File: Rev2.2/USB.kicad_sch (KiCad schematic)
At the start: 3 parts, among them J8 USB_OTG, U6 STMPS2151STR(Current protecti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, U7 USBLC6-2P6(ESD protection)

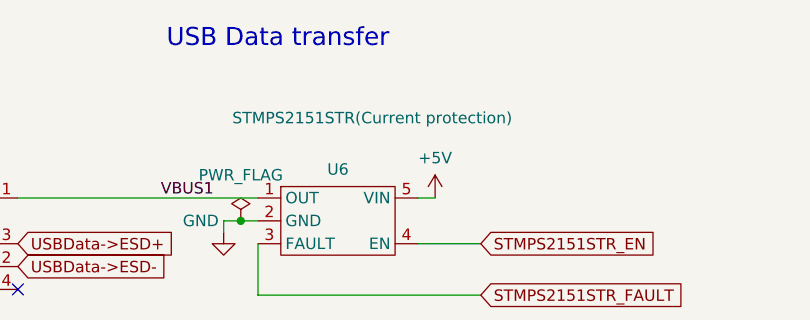
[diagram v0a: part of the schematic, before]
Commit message: changed layer stack up to sig,gnd,gnd, sig/power and routing according to the new stackup
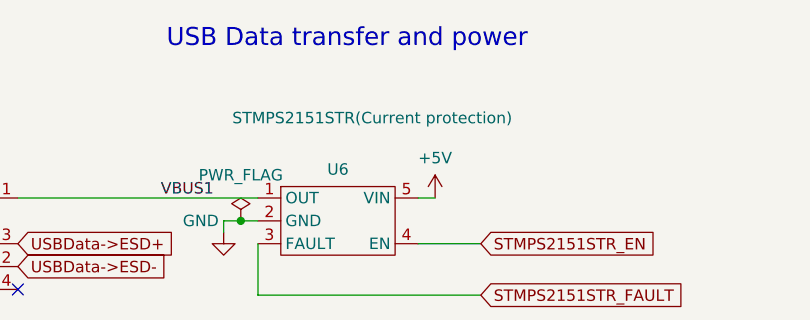
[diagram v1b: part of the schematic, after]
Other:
- note added: "USB Data transfer and power"
- note removed: "USB Data transfer"
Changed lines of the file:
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@@
     )
   )
-  (text "USB Data transfer\n" (at 46.355 19.05 0)
+  (text "USB Data transfer and power\n" (at 46.355 19.05 0)
     (effects (font (size 2 2)) (justify left bottom))
   )

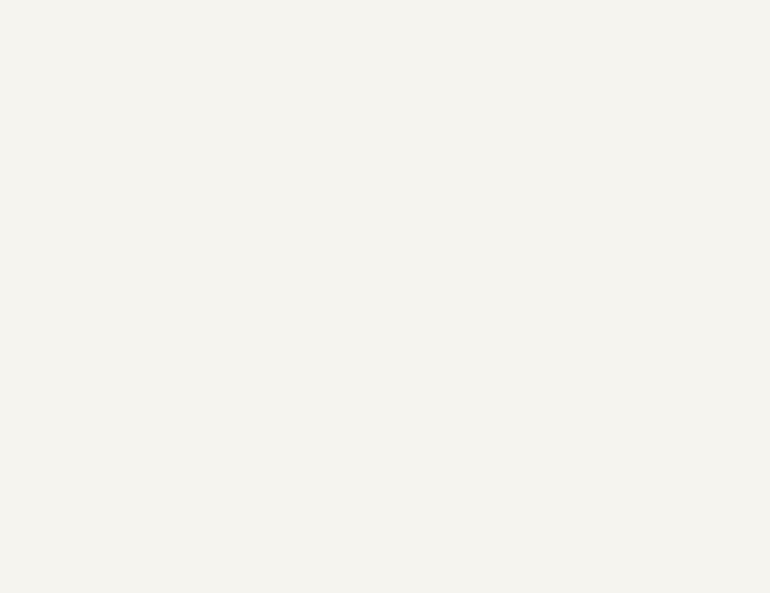
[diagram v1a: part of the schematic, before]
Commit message: added a usb C for power delivery and moved voltage regulator and readjusted the partial power plane to fit the USB C
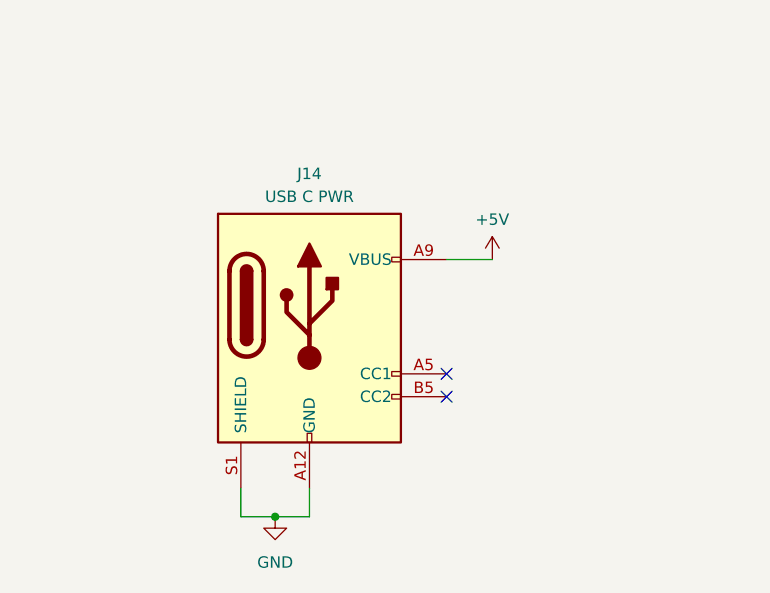
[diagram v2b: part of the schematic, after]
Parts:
- added J14: USB C PWR, Connector_USB:USB_C_Receptacle_GCT_USB4135-GF-A_6P_TopMnt_Horizontal, symbol Connector:USB_C_Receptacle_PowerOnly_6P
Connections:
- net +5V: now also J14.A9 (VBUS), J14.B9 (VBUS)
- net GND: now also J14.A12 (GND), J14.B12 (GND), J14.S1 (SHIELD)
- no-connect marks 1 -> 3
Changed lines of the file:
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@@
   (junction (at 54.61 38.1) (diameter 0) (color 0 0 0 0)
   )
+  (junction (at 40.64 163.83) (diameter 0) (color 0 0 0 0)
+  )
   (junction (at 22.225 53.975) (diameter 0) (color 0 0 0 0)
   )
+  (no_connect (at 59.69 150.495))
+  (no_connect (at 59.69 147.955))
   (no_connect (at 29.845 45.72))
   (wire (pts (xy 52.705 39.37) (xy 52.705 38.1))
     (stroke (width 0) (type default))
   )
+  (wire (pts (xy 40.64 163.83) (xy 44.45 163.83))
+    (stroke (width 0) (type default))
+  )
   (wire (pts (xy 22.225 55.245) (xy 22.225 53.975))
     (stroke (width 0) (type default))
   )
+  (wire (pts (xy 44.45 160.655) (xy 44.45 163.83))
+    (stroke (width 0) (type default))
+  )
   (polyline (pts (xy 12.065 89.535) (xy 285.115 89.535))
     (stroke (width 0) (type default))
@@
     (stroke (width 0) (type default))
   )
+  (wire (pts (xy 36.83 163.83) (xy 40.64 163.83))
+    (stroke (width 0) (type default))
+  )
   (wire (pts (xy 180.34 50.165) (xy 180.34 48.895))
     (stroke (width 0) (type default))
@@
     (stroke (width 0) (type default))
   )
+  (wire (pts (xy 64.77 135.255) (xy 59.69 135.255))
+    (stroke (width 0) (type default))
+  )
   (wire (pts (xy 163.83 38.735) (xy 167.64 38.735))
     (stroke (width 0) (type default))
@@
     (stroke (width 0) (type default))
   )
+  (wire (pts (xy 36.83 160.655) (xy 36.83 163.83))
+    (stroke (width 0) (type default))
+  )
   (wire (pts (xy 52.705 38.1) (xy 54.61 38.1))
     (stroke (width 0) (type default))
@@
     )
   )
+  (symbol (lib_id "Connector:USB_C_Receptacle_PowerOnly_6P") (at 44.45 142.875 0) (unit 1)
+    (in_bom yes) (on_board yes) (dnp no) (fields_autoplaced)
+    (property "Reference" "J14" (at 44.45 125.73 0)
+      (effects (font (size 1.27 1.27)))
+    )
+    (property "Value" "USB C PWR" (at 44.45 128.27 0)
+      (effects (font (size 1.27 1.27)))
+    )
+    (property "Footprint" "Connector_USB:USB_C_Receptacle_GCT_USB4135-GF-A_6P_TopMnt_Horizontal" (at 48.26 140.335 0)
+      (effects (font (size 1.27 1.27)) hide)
+    )
+    (property "Datasheet" "https://www.usb.org/sites/default/files/documents/usb_type-c.zip" (at 44.45 142.875 0)
+      (effects (font (size 1.27 1.27)) hide)
+    )
+    (pin "A12")
+    (pin "A5")
+    (pin "A9")
+    (pin "B12")
+    (pin "B5")
+    (pin "B9")
+    (pin "S1")
+    (instances
+      (project "Rev2.2"
+        (path "/e13dd0ba-f8fd-4ca9-a3d0-94442596488c/4fad712d-8773-4615-bfba-e4cd5d9a6bf4"
+          (reference "J14") (unit 1)
+        )
+      )
+    )
+  )
   (symbol (lib_id "power:GND") (at 22.225 55.245 0) (unit 1)
     (in_bom yes) (on_board yes) (dnp no) (fields_autoplaced)
@@
         )
       )
+    )
+  )
+  (symbol (lib_id "power:+5V") (at 64.77 135.255 0) (unit 1)
+    (in_bom yes) (on_board yes) (dnp no) (fields_autoplaced)
+    (property "Reference" "#PWR059" (at 64.77 139.065 0)
+      (effects (font (size 1.27 1.27)) hide)
+    )
+    (property "Value" "+5V" (at 64.77 130.81 0)
+      (effects (font (size 1.27 1.27)))
+    )
+    (property "Footprint" "" (at 64.77 135.255 0)
+      (effects (font (size 1.27 1.27)) hide)
+    )
+    (property "Datasheet" "" (at 64.77 135.255 0)
+      (effects (font (size 1.27 1.27)) hide)
+    )
+    (pin "1")
+    (instances
+      (project "Rev2.2"
+        (path "/e13dd0ba-f8fd-4ca9-a3d0-94442596488c/4fad712d-8773-4615-bfba-e4cd5d9a6bf4"
+          (reference "#PWR059") (unit 1)
+        )
+      )
+    )
+  )
+  (symbol (lib_id "power:GND") (at 40.64 163.83 0) (unit 1)
+    (in_bom yes) (on_board yes) (dnp no) (fields_autoplaced)
+    (property "Reference" "#PWR060" (at 40.64 170.18 0)
+      (effects (font (size 1.27 1.27)) hide)
+    )
+    (property "Value" "GND" (at 40.64 168.91 0)
+      (effects (font (size 1.27 1.27)))
+    )
+    (property "Footprint" "" (at 40.64 163.83 0)
+      (effects (font (size 1.27 1.27)) hide)
+    )
+    (property "Datasheet" "" (at 40.64 163.83 0)
+      (effects (font (size 1.27 1.27)) hide)
+    )
+    (pin "1")
+    (instances
+      (project "Rev2.2"
+        (path "/e13dd0ba-f8fd-4ca9-a3d0-94442596488c/4fad712d-8773-4615-bfba-e4cd5d9a6bf4"
+          (reference "#PWR060") (unit 1)
+        )
+      )

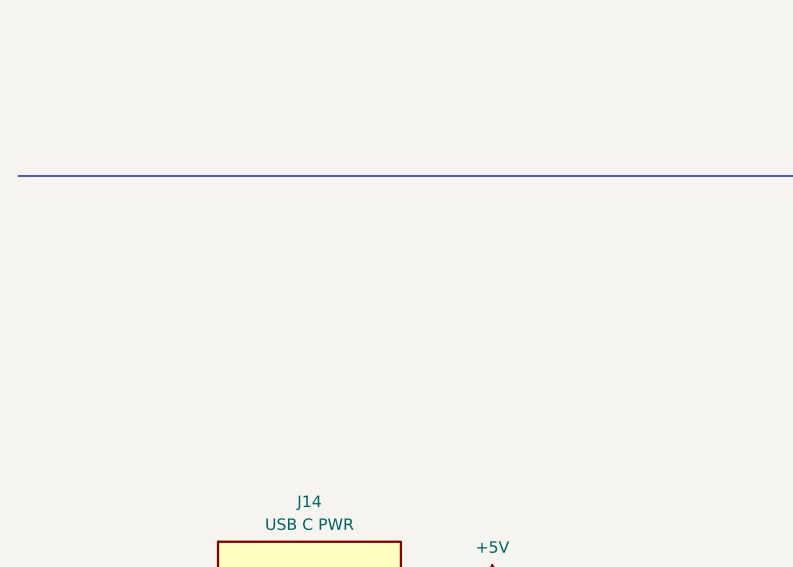
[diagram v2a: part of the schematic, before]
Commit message: added manufacturing files
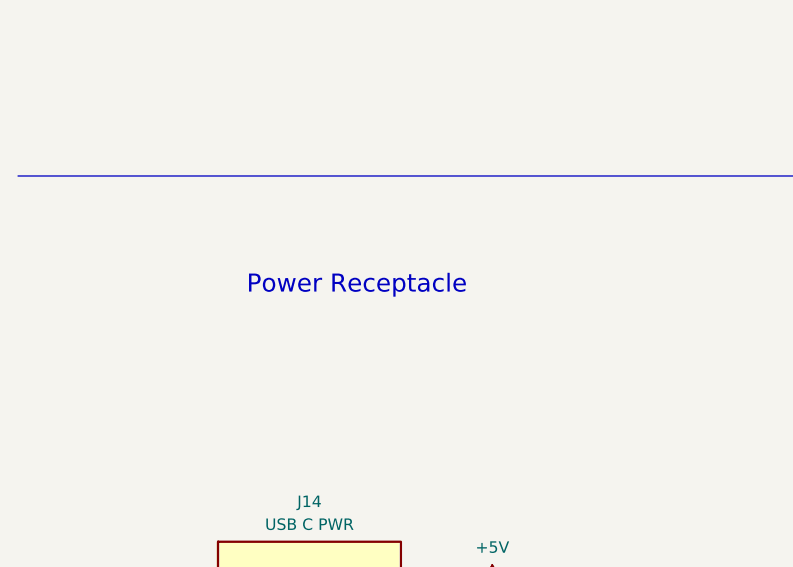
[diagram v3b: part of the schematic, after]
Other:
- note added: "Power Receptacle"
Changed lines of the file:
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@@
     )
+  )
+  (text "Power Receptacle\n" (at 37.465 102.87 0)
+    (effects (font (size 2 2)) (justify left bottom))
   )
   (text "USB Data transfer and power\n" (at 46.355 19.05 0)
